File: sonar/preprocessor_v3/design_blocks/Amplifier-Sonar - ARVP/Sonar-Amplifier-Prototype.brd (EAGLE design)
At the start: 20 x 20 mm, 20 parts, among them U1 AD8336ACPZ-R7

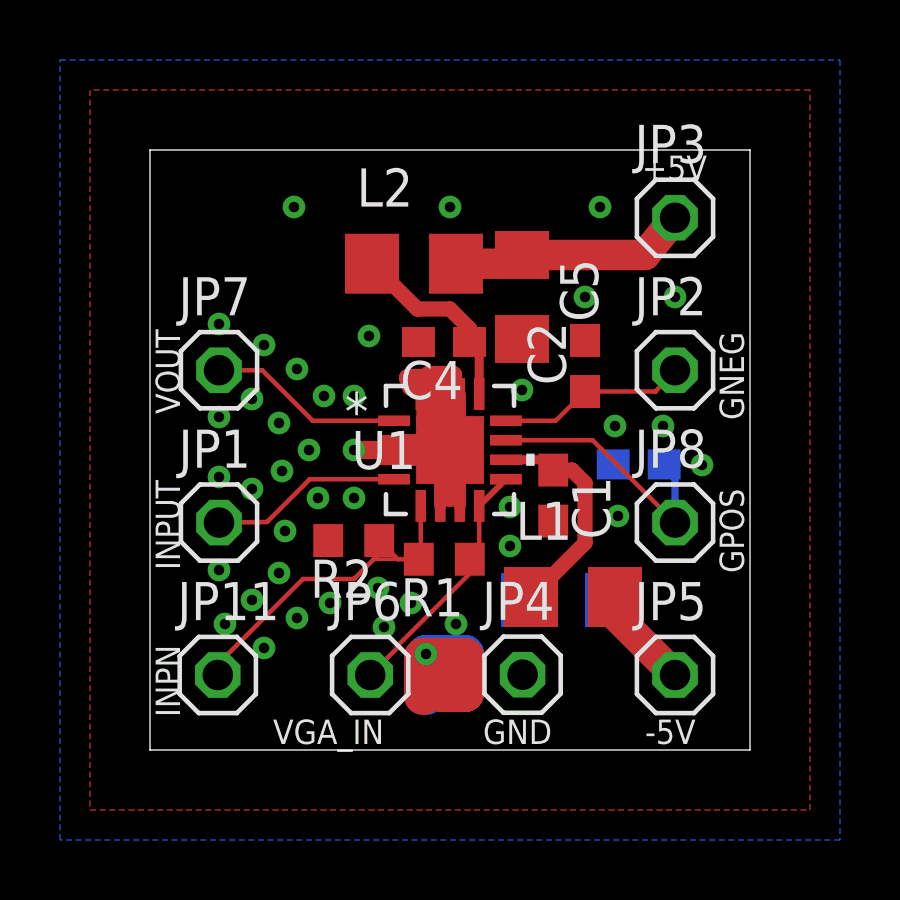
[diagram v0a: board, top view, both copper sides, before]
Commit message: Renamed files
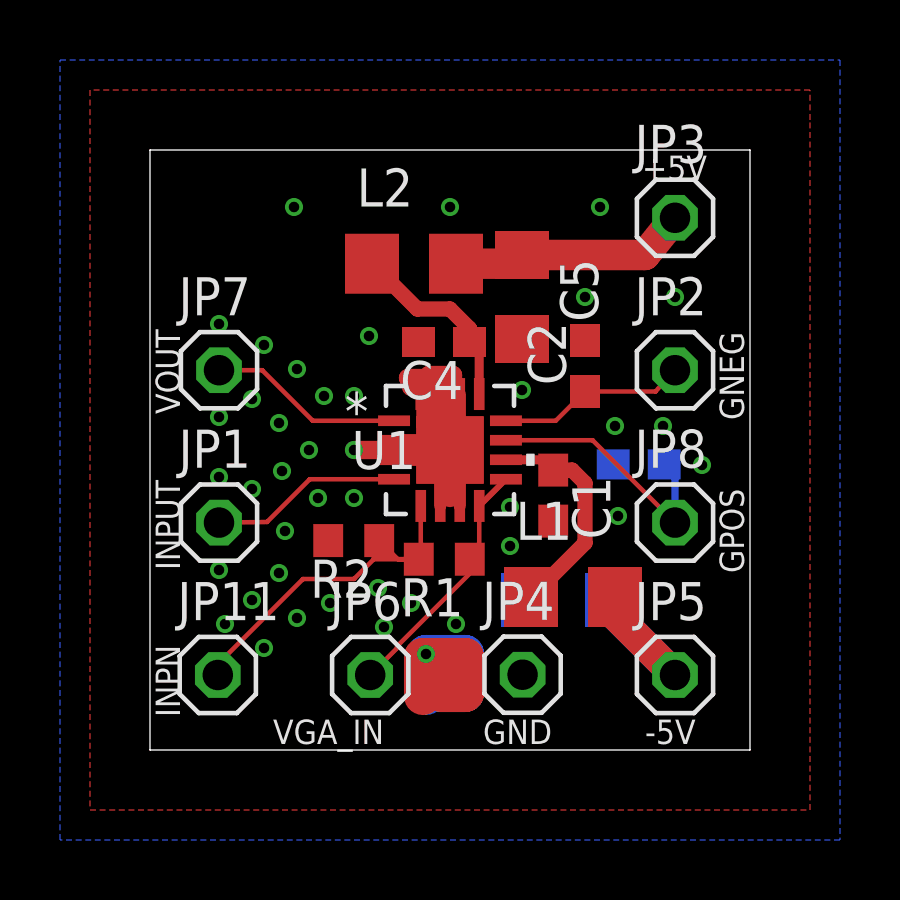
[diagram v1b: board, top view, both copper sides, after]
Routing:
- net INPN: track 12.6 -> 13.3 mm
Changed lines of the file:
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@@
 <?xml version="1.0" encoding="utf-8"?>
 <!DOCTYPE eagle SYSTEM "eagle.dtd">
-<eagle version="8.6.0">
+<eagle version="8.6.1">
 <drawing>
 <settings>
@@
 </class>
 </classes>
-<designrules name="default">
+<designrules name="OSHPark2Layer">
 <description language="de">&lt;b&gt;EAGLE Design Rules&lt;/b&gt;
 &lt;p&gt;
@@
 necessary adjustments and save your customized
 design rules under a new name.</description>
+<description language="zh">&lt;b&gt;Seeed Studio EAGLE Design Rules&lt;/b&gt;
+</description>
 <param name="layerSetup" value="(1*16)"/>
 <param name="mtCopper" value="0.035mm 0.035mm 0.035mm 0.035mm 0.035mm 0.035mm 0.035mm 0.035mm 0.035mm 0.035mm 0.035mm 0.035mm 0.035mm 0.035mm 0.035mm 0.035mm"/>
@@
 <param name="mdPadVia" value="6mil"/>
 <param name="mdViaVia" value="6mil"/>
-<param name="mdSmdPad" value="6mil"/>
-<param name="mdSmdVia" value="6mil"/>
-<param name="mdSmdSmd" value="6mil"/>
-<param name="mdViaViaSameLayer" value="6mil"/>
+<param name="mdSmdPad" value="0mil"/>
+<param name="mdSmdVia" value="0mil"/>
+<param name="mdSmdSmd" value="0mil"/>
+<param name="mdViaViaSameLayer" value="8mil"/>
 <param name="mnLayersViaInSmd" value="2"/>
-<param name="mdCopperDimension" value="40mil"/>
-<param name="mdDrill" value="6mil"/>
+<param name="mdCopperDimension" value="10mil"/>
+<param name="mdDrill" value="10mil"/>
 <param name="mdSmdStop" value="0mil"/>
 <param name="msWidth" value="6mil"/>
-<param name="msDrill" value="0.35mm"/>
-<param name="msMicroVia" value="9.99mm"/>
+<param name="msDrill" value="10mil"/>
+<param name="msMicroVia" value="10mil"/>
 <param name="msBlindViaRatio" value="0.5"/>
 <param name="rvPadTop" value="0.25"/>
@@
 <param name="rvMicroViaOuter" value="0.25"/>
 <param name="rvMicroViaInner" value="0.25"/>
-<param name="rlMinPadTop" value="10mil"/>
+<param name="rlMinPadTop" value="5mil"/>
 <param name="rlMaxPadTop" value="20mil"/>
-<param name="rlMinPadInner" value="10mil"/>
+<param name="rlMinPadInner" value="5mil"/>
 <param name="rlMaxPadInner" value="20mil"/>
-<param name="rlMinPadBottom" value="10mil"/>
+<param name="rlMinPadBottom" value="5mil"/>
 <param name="rlMaxPadBottom" value="20mil"/>
-<param name="rlMinViaOuter" value="8mil"/>
+<param name="rlMinViaOuter" value="5mil"/>
 <param name="rlMaxViaOuter" value="20mil"/>
-<param name="rlMinViaInner" value="8mil"/>
+<param name="rlMinViaInner" value="5mil"/>
 <param name="rlMaxViaInner" value="20mil"/>
 <param name="rlMinMicroViaOuter" value="4mil"/>
@@
 <param name="psTop" value="-1"/>
 <param name="psBottom" value="-1"/>
-<param name="psFirst" value="-1"/>
+<param name="psFirst" value="0"/>
 <param name="psElongationLong" value="100"/>
 <param name="psElongationOffset" value="100"/>
 <param name="mvStopFrame" value="1"/>
 <param name="mvCreamFrame" value="0"/>
-<param name="mlMinStopFrame" value="4mil"/>
-<param name="mlMaxStopFrame" value="4mil"/>
+<param name="mlMinStopFrame" value="2mil"/>
+<param name="mlMaxStopFrame" value="2mil"/>
 <param name="mlMinCreamFrame" value="0mil"/>
 <param name="mlMaxCreamFrame" value="0mil"/>
-<param name="mlViaStopLimit" value="0mil"/>
+<param name="mlViaStopLimit" value="100mil"/>
 <param name="srRoundness" value="0"/>
 <param name="srMinRoundness" value="0mil"/>
@@
 <param name="checkAngle" value="0"/>
 <param name="checkFont" value="1"/>
-<param name="checkRestrict" value="1"/>
+<param name="checkRestrict" value="0"/>
 <param name="checkStop" value="0"/>
 <param name="checkValues" value="0"/>
@@
 <wire x1="8.6" y1="12.4" x2="8.7" y2="12.3" width="0.6096" layer="1" curve="-90"/>
 <wire x1="8.7" y1="12.3" x2="8.7" y2="12.1" width="0.6096" layer="1"/>
-<wire x1="8.7" y1="12.4" x2="8.7" y2="12.1903" width="0.127" layer="1"/>
+<wire x1="8.7" y1="12.4" x2="8.7" y2="12.1903" width="0.1524" layer="1"/>
 <wire x1="8.7" y1="12.1903" x2="9.025" y2="11.8653" width="0.127" layer="1"/>
-<wire x1="10" y1="10" x2="9.3" y2="10.7" width="0.127" layer="1"/>
-<wire x1="9.3" y1="10.7" x2="9.3" y2="11" width="0.127" layer="1"/>
+<wire x1="10" y1="10" x2="9.3" y2="10.7" width="0.1524" layer="1"/>
+<wire x1="9.3" y1="10.7" x2="9.3" y2="11" width="0.1524" layer="1"/>
 </signal>
 <signal name="+5V">
@@
 <wire x1="8.26" y1="6.36" x2="7.64" y2="6.98" width="0.1524" layer="1"/>
 <wire x1="7.64" y1="6.98" x2="7.64" y2="6.54" width="0.1524" layer="1"/>
-<wire x1="7.64" y1="6.54" x2="7.45" y2="6.35" width="0.1524" layer="1"/>
+<wire x1="7.64" y1="6.54" x2="7.46" y2="6.36" width="0.1524" layer="1"/>
 <wire x1="7.45" y1="6.35" x2="6.8" y2="5.7" width="0.1524" layer="1"/>
 <wire x1="6.8" y1="5.7" x2="5.1" y2="5.7" width="0.1524" layer="1"/>
 <wire x1="5.1" y1="5.7" x2="2.3" y2="2.9" width="0.1524" layer="1"/>
 <wire x1="2.3" y1="2.9" x2="2.26" y2="2.5" width="0.1524" layer="1"/>
-<wire x1="8.96" y1="6.36" x2="7.46" y2="6.36" width="0.127" layer="1"/>
-<wire x1="7.46" y1="6.36" x2="7.45" y2="6.35" width="0.127" layer="1"/>
+<wire x1="8.96" y1="6.36" x2="7.46" y2="6.36" width="0.1524" layer="1"/>
+<wire x1="7.46" y1="6.36" x2="7.45" y2="6.35" width="0.1524" layer="1"/>
+<wire x1="7.46" y1="6.36" x2="7.46" y2="6.8" width="0.1524" layer="1"/>
+<wire x1="7.46" y1="6.8" x2="7.64" y2="6.98" width="0.1524" layer="1"/>
 </signal>
 </signals>
